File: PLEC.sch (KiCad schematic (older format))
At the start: 13 parts, among them J1 Conn_01x02, J2 Conn_01x02, J3 Conn_01x06, J4 Conn_01x04, J5 Conn_01x03

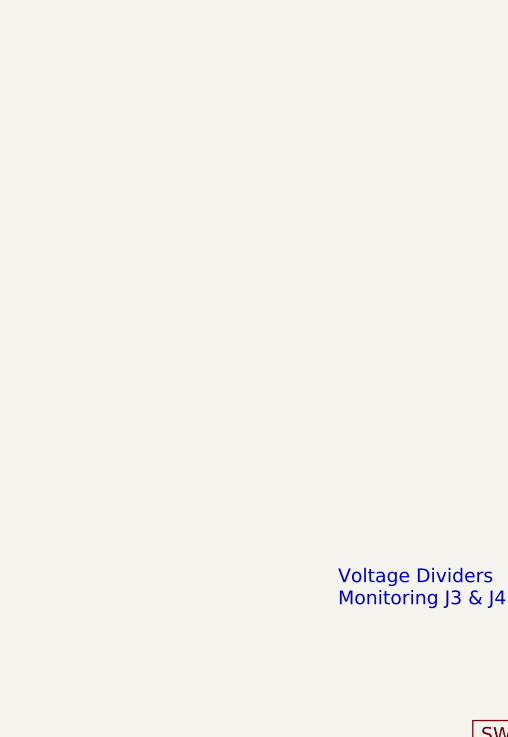
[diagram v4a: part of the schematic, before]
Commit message: Stiched vias and added mounting holes with no errors
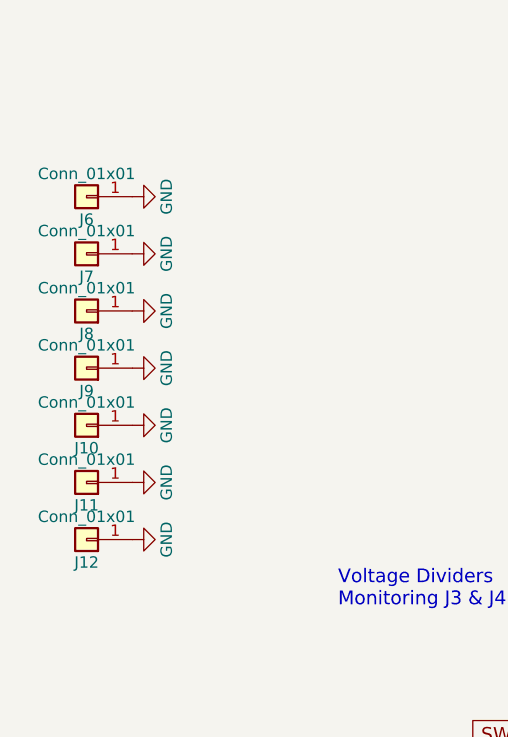
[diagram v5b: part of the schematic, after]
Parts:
- added J10, J11, J6, J7, J8, J9: Conn_01x01, PLEC:Hole4-40, symbol Conn_01x01
- added J12: Conn_01x01, PLEC:Via-0.6mm, symbol Conn_01x01
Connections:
- net GND: now also J10.1 (Pin_1), J11.1 (Pin_1), J12.1 (Pin_1), J6.1 (Pin_1), J7.1 (Pin_1), J8.1 (Pin_1), J9.1 (Pin_1)
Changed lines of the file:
@@
 Wire Wire Line
 	3100 6000 2900 6000
+$Comp
+L Conn_01x01 J6
+U 1 1 5A873216
+P 850 2850
+F 0 "J6" H 850 2950 50  0000 C CNN
+F 1 "Conn_01x01" H 850 2750 50  0000 C CNN
+F 2 "PLEC:Hole4-40" H 850 2850 50  0001 C CNN
+F 3 "" H 850 2850 50  0001 C CNN
+	1    850  2850
+	-1   0    0    1
+$EndComp
+$Comp
+L Conn_01x01 J7
+U 1 1 5A873569
+P 850 3100
+F 0 "J7" H 850 3200 50  0000 C CNN
+F 1 "Conn_01x01" H 850 3000 50  0000 C CNN
+F 2 "PLEC:Hole4-40" H 850 3100 50  0001 C CNN
+F 3 "" H 850 3100 50  0001 C CNN
+	1    850  3100
+	-1   0    0    1
+$EndComp
+$Comp
+L Conn_01x01 J8
+U 1 1 5A873840
+P 850 3350
+F 0 "J8" H 850 3450 50  0000 C CNN
+F 1 "Conn_01x01" H 850 3250 50  0000 C CNN
+F 2 "PLEC:Hole4-40" H 850 3350 50  0001 C CNN
+F 3 "" H 850 3350 50  0001 C CNN
+	1    850  3350
+	-1   0    0    1
+$EndComp
+$Comp
+L Conn_01x01 J9
+U 1 1 5A873B0E
+P 850 3600
+F 0 "J9" H 850 3700 50  0000 C CNN
+F 1 "Conn_01x01" H 850 3500 50  0000 C CNN
+F 2 "PLEC:Hole4-40" H 850 3600 50  0001 C CNN
+F 3 "" H 850 3600 50  0001 C CNN
+	1    850  3600
+	-1   0    0    1
+$EndComp
+$Comp
+L Conn_01x01 J10
+U 1 1 5A873DE1
+P 850 3850
+F 0 "J10" H 850 3950 50  0000 C CNN
+F 1 "Conn_01x01" H 850 3750 50  0000 C CNN
+F 2 "PLEC:Hole4-40" H 850 3850 50  0001 C CNN
+F 3 "" H 850 3850 50  0001 C CNN
+	1    850  3850
+	-1   0    0    1
+$EndComp
+$Comp
+L Conn_01x01 J11
+U 1 1 5A8740B5
+P 850 4100
+F 0 "J11" H 850 4200 50  0000 C CNN
+F 1 "Conn_01x01" H 850 4000 50  0000 C CNN
+F 2 "PLEC:Hole4-40" H 850 4100 50  0001 C CNN
+F 3 "" H 850 4100 50  0001 C CNN
+	1    850  4100
+	-1   0    0    1
+$EndComp
+$Comp
+L Conn_01x01 J12
+U 1 1 5A87438C
+P 850 4350
+F 0 "J12" H 850 4450 50  0000 C CNN
+F 1 "Conn_01x01" H 850 4250 50  0000 C CNN
+F 2 "PLEC:Via-0.6mm" H 850 4350 50  0001 C CNN
+F 3 "" H 850 4350 50  0001 C CNN
+	1    850  4350
+	-1   0    0    1
+$EndComp
+$Comp
+L GND #PWR05
+U 1 1 5A8747C2
+P 1050 2850
+F 0 "#PWR05" H 1050 2600 50  0001 C CNN
+F 1 "GND" H 1050 2700 50  0000 C CNN
+F 2 "" H 1050 2850 50  0001 C CNN
+F 3 "" H 1050 2850 50  0001 C CNN
+	1    1050 2850
+	0    -1   -1   0
+$EndComp
+$Comp
+L GND #PWR06
+U 1 1 5A874A91
+P 1050 3100
+F 0 "#PWR06" H 1050 2850 50  0001 C CNN
+F 1 "GND" H 1050 2950 50  0000 C CNN
+F 2 "" H 1050 3100 50  0001 C CNN
+F 3 "" H 1050 3100 50  0001 C CNN
+	1    1050 3100
+	0    -1   -1   0
+$EndComp
+$Comp
+L GND #PWR07
+U 1 1 5A874D60
+P 1050 3350
+F 0 "#PWR07" H 1050 3100 50  0001 C CNN
+F 1 "GND" H 1050 3200 50  0000 C CNN
+F 2 "" H 1050 3350 50  0001 C CNN
+F 3 "" H 1050 3350 50  0001 C CNN
+	1    1050 3350
+	0    -1   -1   0
+$EndComp
+$Comp
+L GND #PWR08
+U 1 1 5A87502F
+P 1050 3600
+F 0 "#PWR08" H 1050 3350 50  0001 C CNN
+F 1 "GND" H 1050 3450 50  0000 C CNN
+F 2 "" H 1050 3600 50  0001 C CNN
+F 3 "" H 1050 3600 50  0001 C CNN
+	1    1050 3600
+	0    -1   -1   0
+$EndComp
+$Comp
+L GND #PWR09
+U 1 1 5A875B68
+P 1050 3850
+F 0 "#PWR09" H 1050 3600 50  0001 C CNN
+F 1 "GND" H 1050 3700 50  0000 C CNN
+F 2 "" H 1050 3850 50  0001 C CNN
+F 3 "" H 1050 3850 50  0001 C CNN
+	1    1050 3850
+	0    -1   -1   0
+$EndComp
+$Comp
+L GND #PWR010
+U 1 1 5A875E37
+P 1050 4100
+F 0 "#PWR010" H 1050 3850 50  0001 C CNN
+F 1 "GND" H 1050 3950 50  0000 C CNN
+F 2 "" H 1050 4100 50  0001 C CNN
+F 3 "" H 1050 4100 50  0001 C CNN
+	1    1050 4100
+	0    -1   -1   0
+$EndComp
+$Comp
+L GND #PWR011
+U 1 1 5A876106
+P 1050 4350
+F 0 "#PWR011" H 1050 4100 50  0001 C CNN
+F 1 "GND" H 1050 4200 50  0000 C CNN
+F 2 "" H 1050 4350 50  0001 C CNN
+F 3 "" H 1050 4350 50  0001 C CNN
+	1    1050 4350
+	0    -1   -1   0
+$EndComp
 $EndSCHEMATC
